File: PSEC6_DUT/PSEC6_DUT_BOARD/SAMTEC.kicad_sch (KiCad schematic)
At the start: 0 parts

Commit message: created ADC buffer schematic
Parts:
- added J1, J2: QTH-040-01-X-D-DP-A, QTH-040-01-X-D-DP-A:SAMTEC_QTH-040-01-X-D-DP-A, symbol QTH_040_01_L_D_DP_A:QTH-040-01-X-D-DP-A
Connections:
- new net VDD12: J2.37, J2.39
- new net VDD18: J2.33, J2.35
- new net VDD25: J2.29, J2.31
- new net VDD33: J2.25, J2.27
- new net VDD50: J2.21, J2.23
- new net VDDCUSTOM: J2.17, J2.19

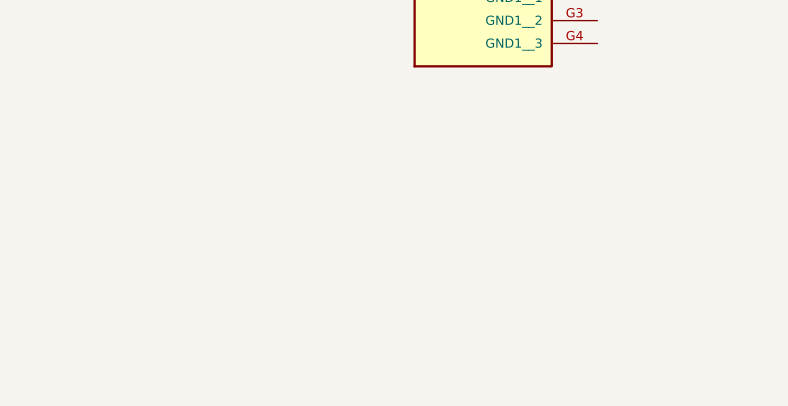
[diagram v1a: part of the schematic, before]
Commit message: Updating values and added RC filters for DUT Card
Added RC filters onto the bias signals and discriminator thresholds, and added RCL values for the SMA devices to provide good DC biasing voltage from the pedestals.
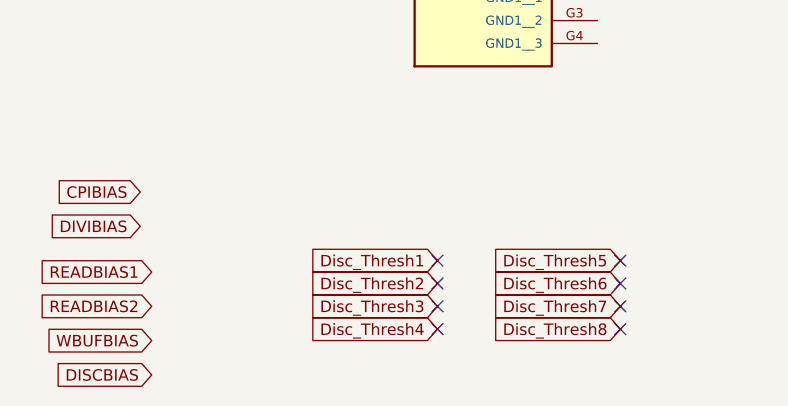
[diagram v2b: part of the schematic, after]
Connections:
- no-connect marks 0 -> 8

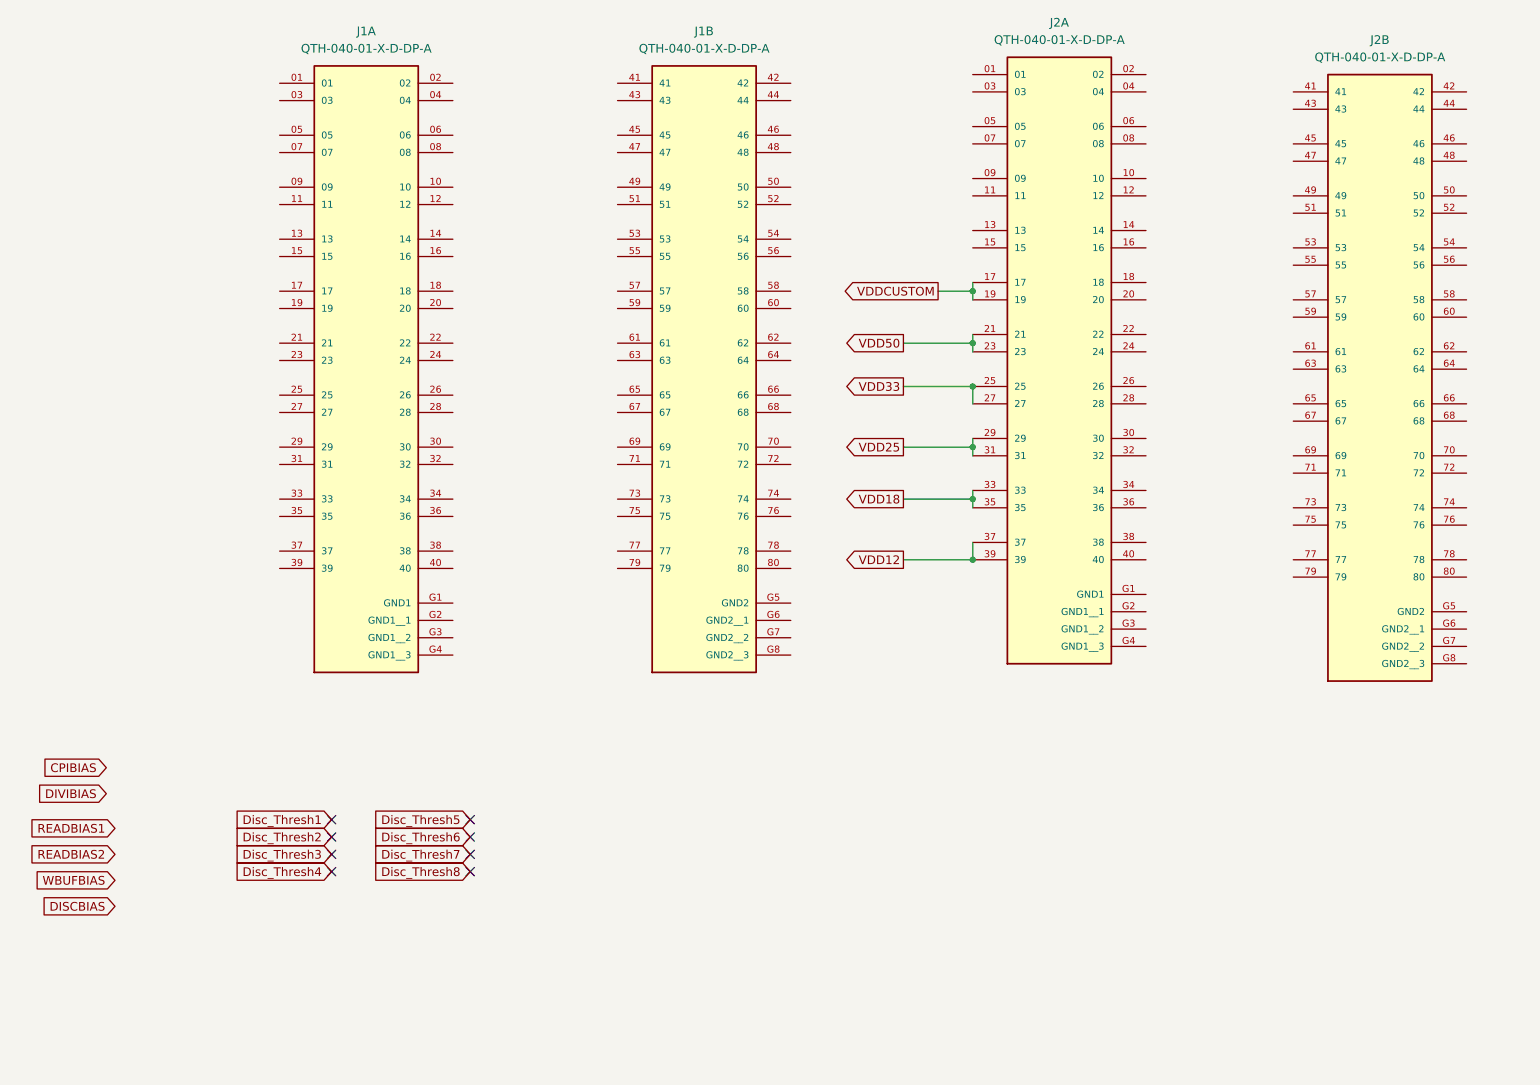
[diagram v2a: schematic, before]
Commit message: DUT Board Schematic Done besides SAMTEC
The DUT Board is now done and fully documented besides the placement of the signals on the SAMTEC connector between the two boards, as the position of each connection will be determined during layout.
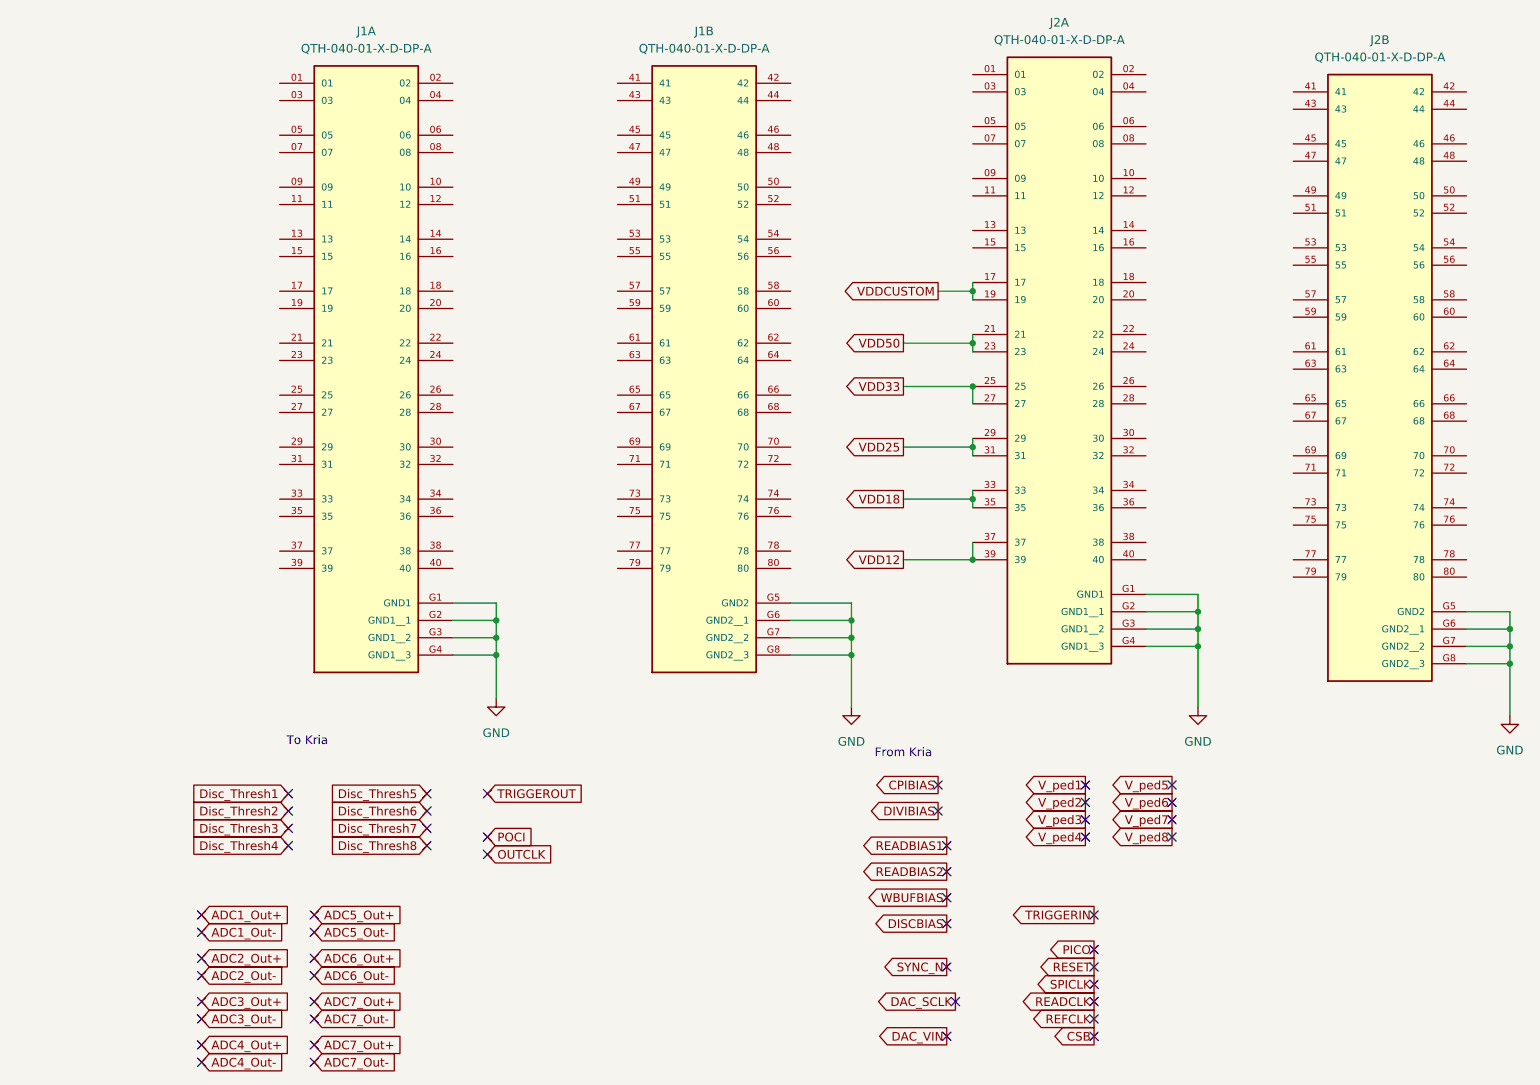
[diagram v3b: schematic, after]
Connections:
- net GND: now reaches J1.G5 (GND2)
- net GND: now also J1.G1 (GND1), J1.G2 (GND1__1), J1.G3 (GND1__2), J1.G4 (GND1__3), J1.G6 (GND2__1), J1.G7 (GND2__2), J1.G8 (GND2__3), J2.G1 (GND1), J2.G2 (GND1__1), J2.G3 (GND1__2), J2.G4 (GND1__3), J2.G5 (GND2), J2.G6 (GND2__1), J2.G7 (GND2__2), J2.G8 (GND2__3)
- no-connect marks 8 -> 51
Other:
- note added: "From Kria"
- note added: "To Kria"

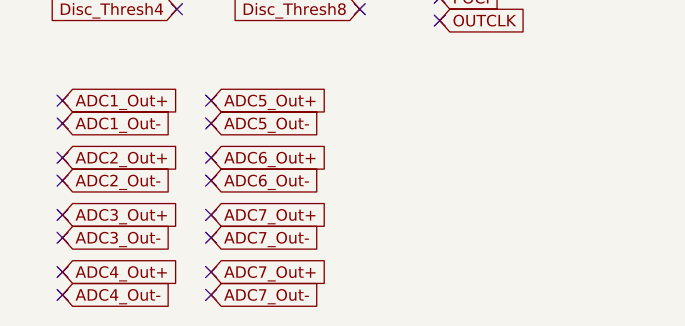
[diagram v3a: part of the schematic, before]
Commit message: Many Updates
Starting new power sequence and implementing KR260 PS circuitry.
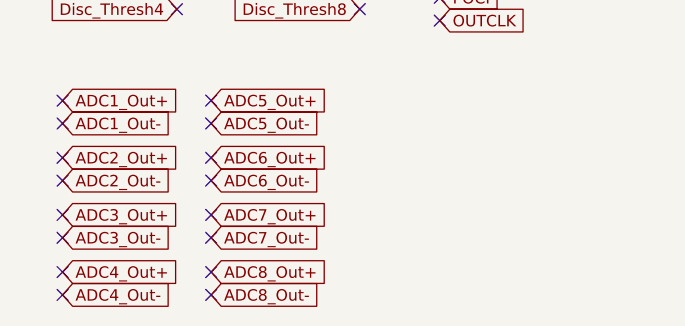
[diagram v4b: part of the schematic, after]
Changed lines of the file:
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@@
 		)
 	)
-	(global_label "ADC7_Out-"
+	(global_label "ADC8_Out-"
 		(shape input)
 		(at 59.69 186.69 0)
@@
 		)
 	)
-	(global_label "ADC7_Out+"
+	(global_label "ADC8_Out+"
 		(shape input)
 		(at 59.69 184.15 0)
